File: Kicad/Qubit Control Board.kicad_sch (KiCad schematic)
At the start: 152 parts, among them J1 USB_C_Receptacle_PowerOnly_6P, J2 CLK_Pins, J3 Idata, J4 Qdata, J5 SPIdata, J6 SMA, U1 LT3045xMSE, U2 TRF372017IRGZR, U3 LT3045xMSE, U4 LT3045xMSE, U5 SN65LVDS1DBV, U6 AD9743BCPZ, Y2 CVHD-950-100.000

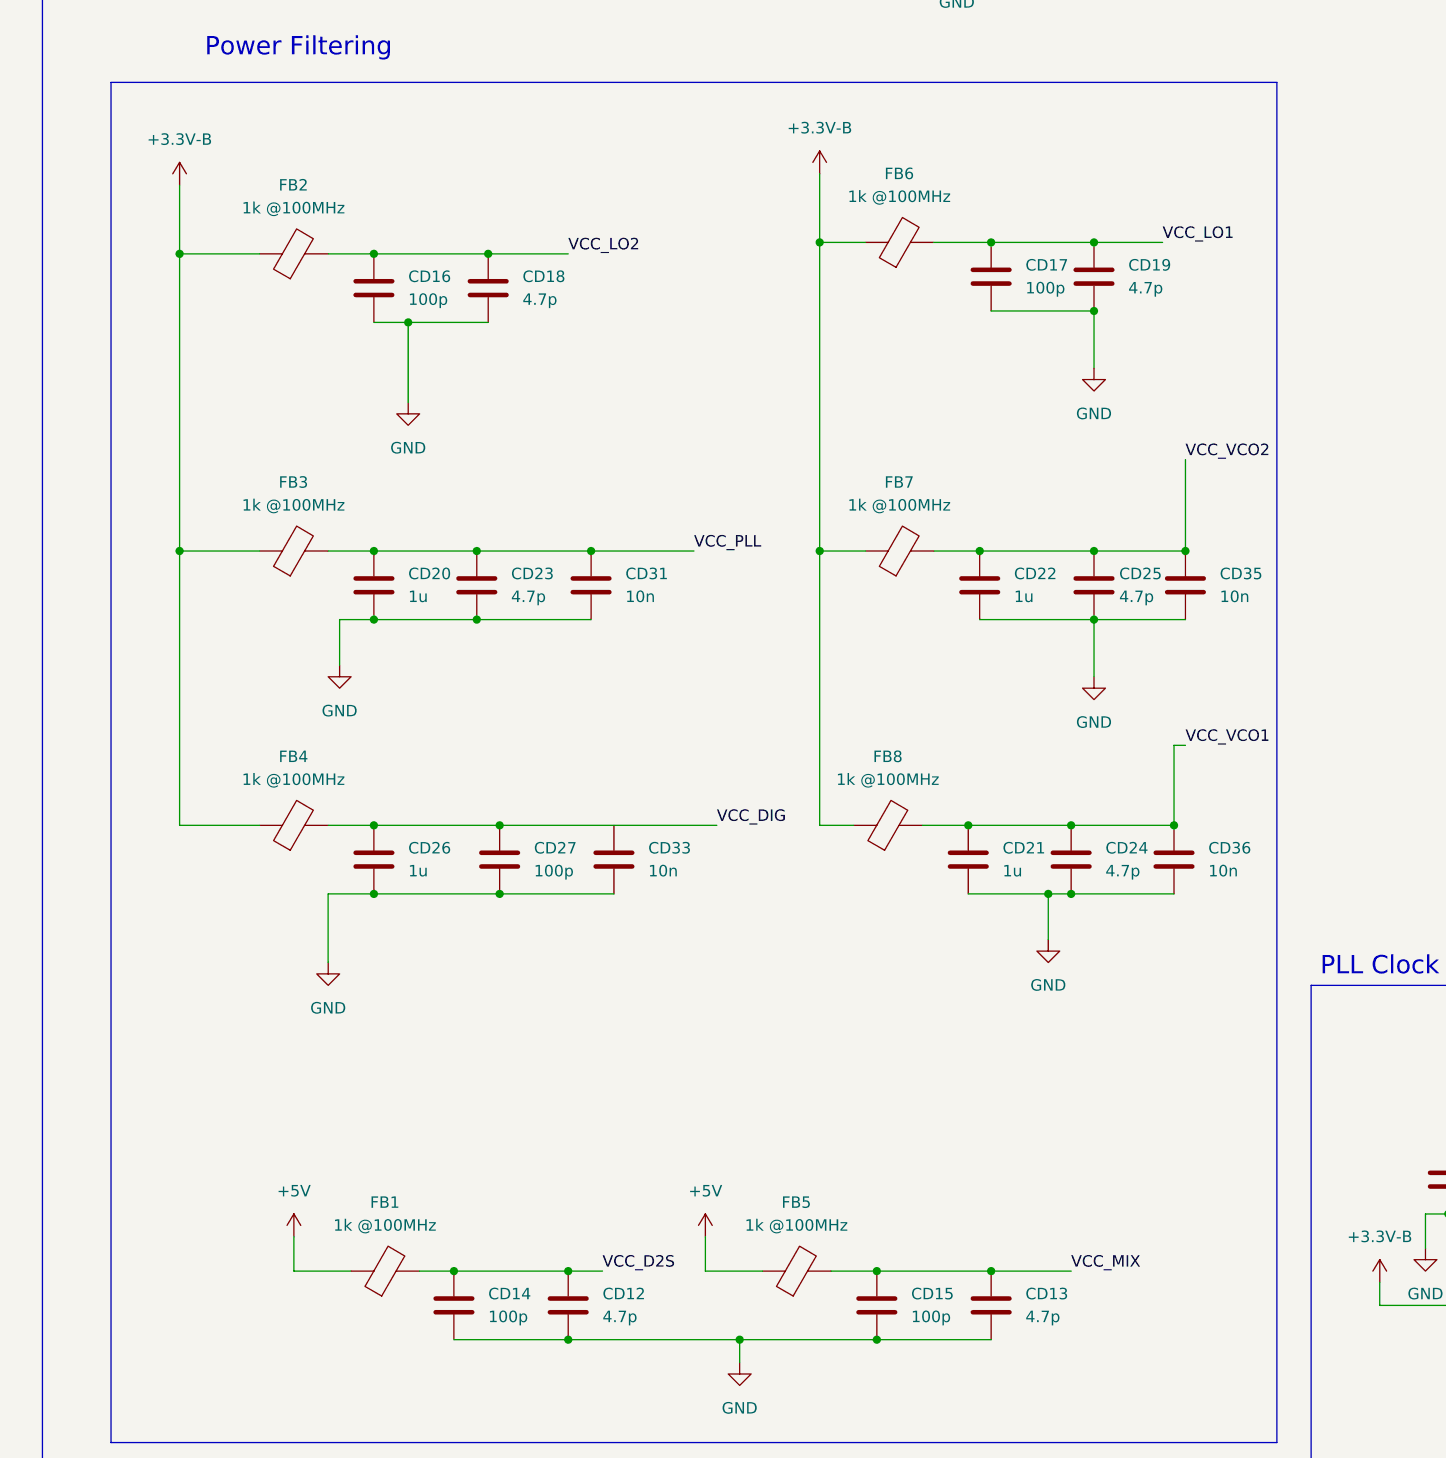
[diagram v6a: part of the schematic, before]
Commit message: added series R to FB to add damping to oss
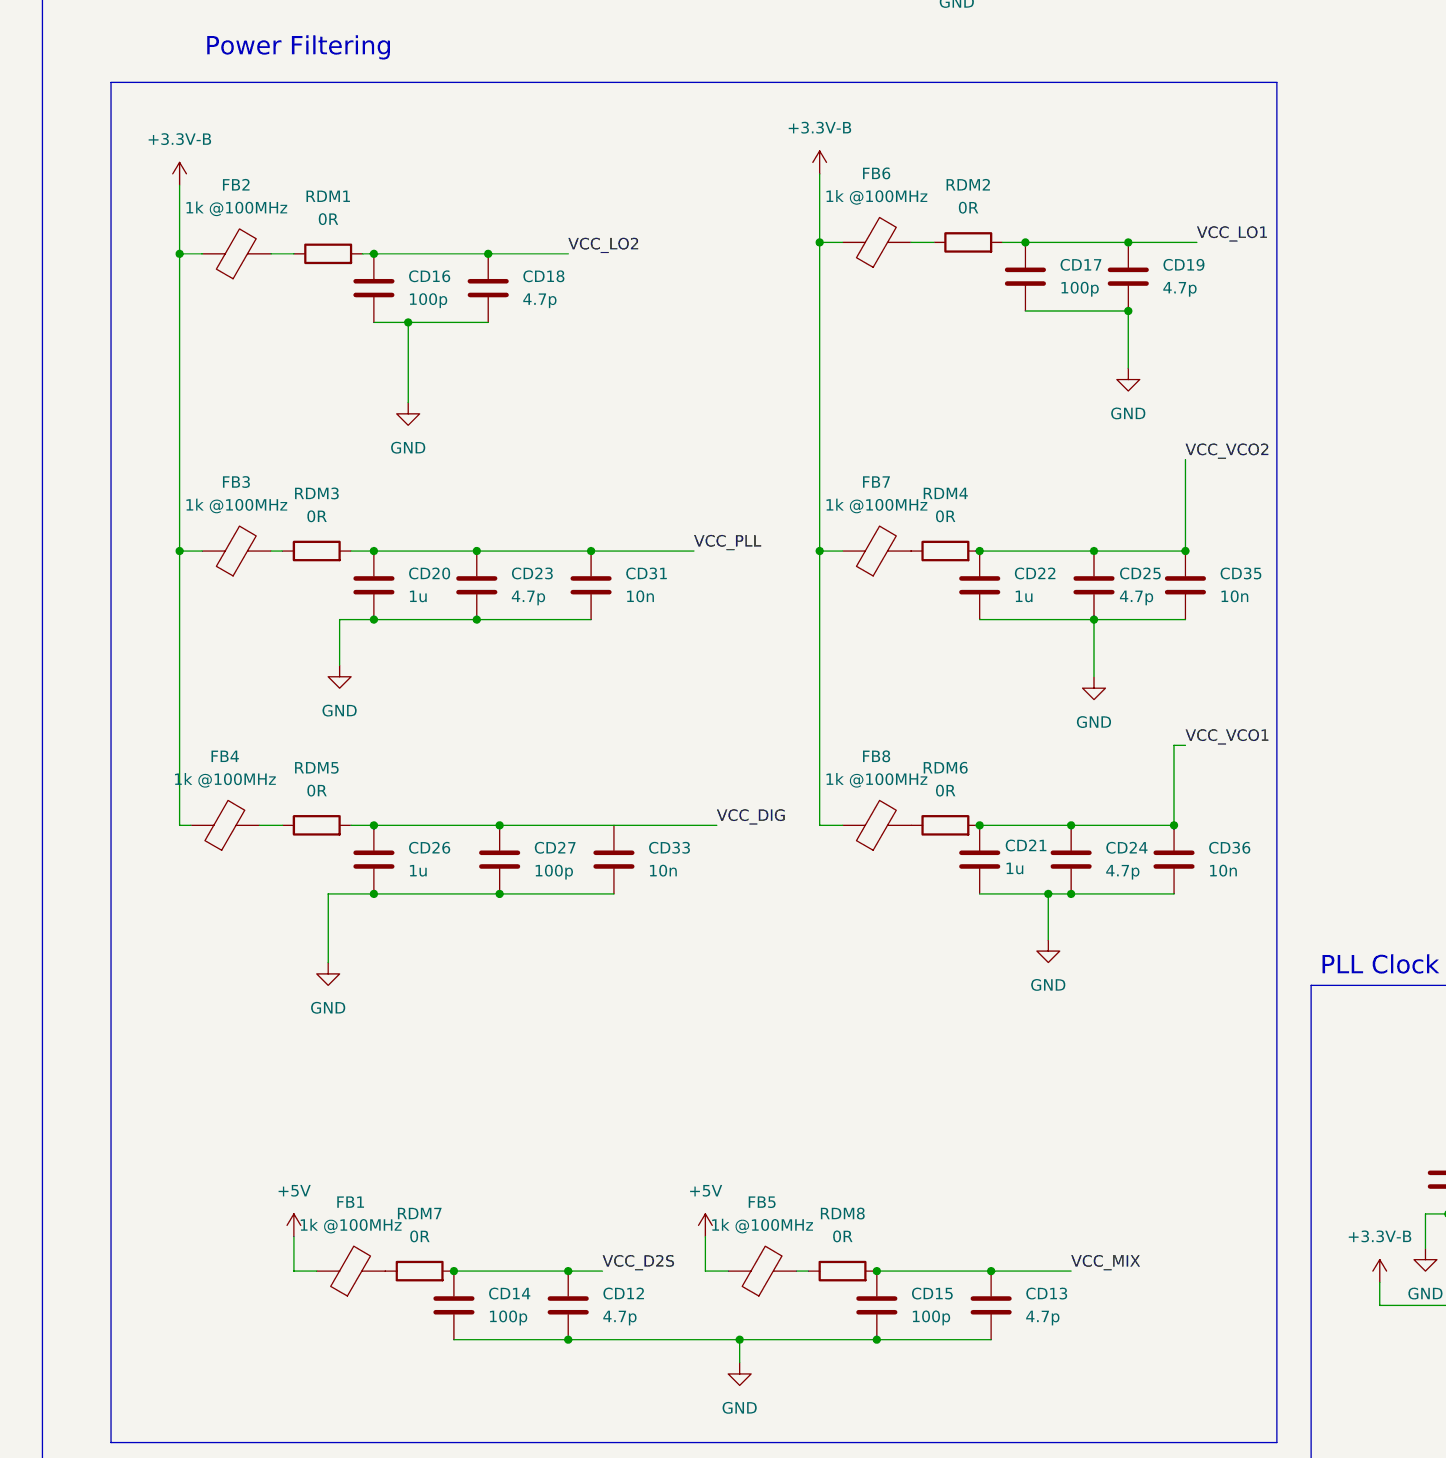
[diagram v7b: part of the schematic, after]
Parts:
- added RDM1, RDM2, RDM3, RDM4, RDM5, RDM6, RDM7, RDM8: 0R, Resistor_SMD:R_0603_1608Metric, symbol Device:R
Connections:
- net VCC_D2S: now also RDM7.2; no longer FB1.2
- net VCC_DIG: now also RDM5.2; no longer FB4.2
- net VCC_LO1: now also RDM2.2; no longer FB6.2
- net VCC_LO2: now also RDM1.2; no longer FB2.2
- net VCC_MIX: now also RDM8.2; no longer FB5.2
- net VCC_PLL: now also RDM3.2; no longer FB3.2
- net VCC_VCO1: now also RDM6.2; no longer FB8.2
- net VCC_VCO2: now also RDM4.2; no longer FB7.2
- new net: FB6.2, RDM2.1
- new net: FB7.2, RDM4.1
- new net: FB5.2, RDM8.1
- new net: FB2.2, RDM1.1
- new net: FB1.2, RDM7.1
- new net: FB4.2, RDM5.1
- new net: FB3.2, RDM3.1
- new net: FB8.2, RDM6.1
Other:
- moved on the sheet: CD17, CD19, CD21, FB1, FB2, FB3, FB4, FB5, FB6, FB7, FB8

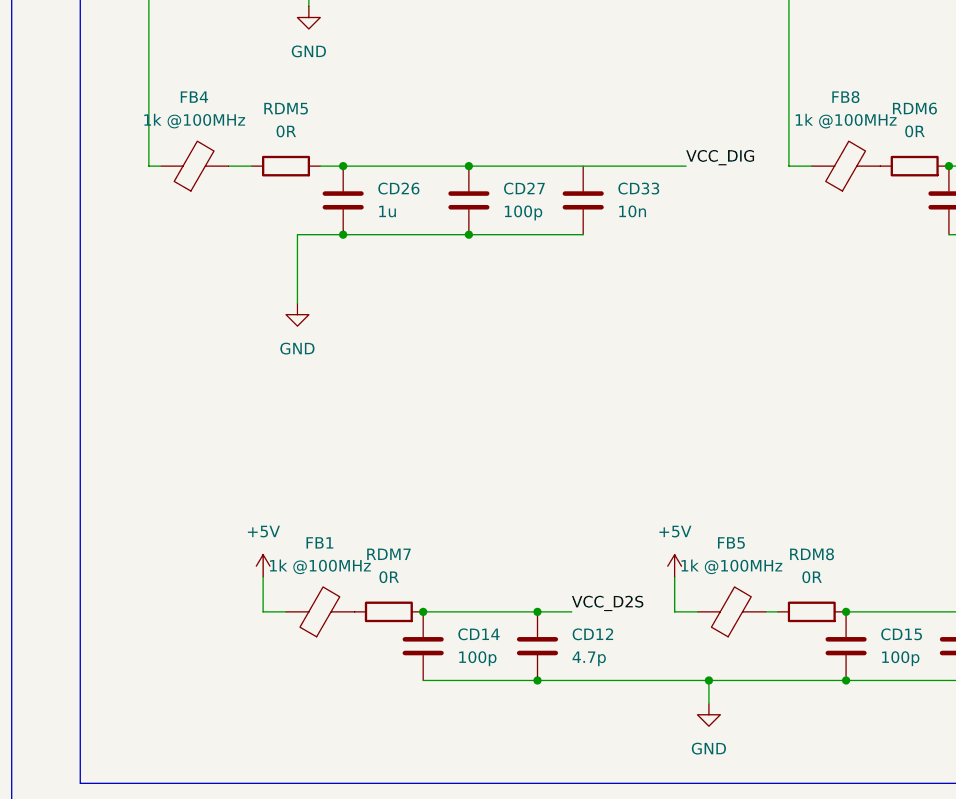
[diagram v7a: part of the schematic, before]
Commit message: REREF routing with on board clock
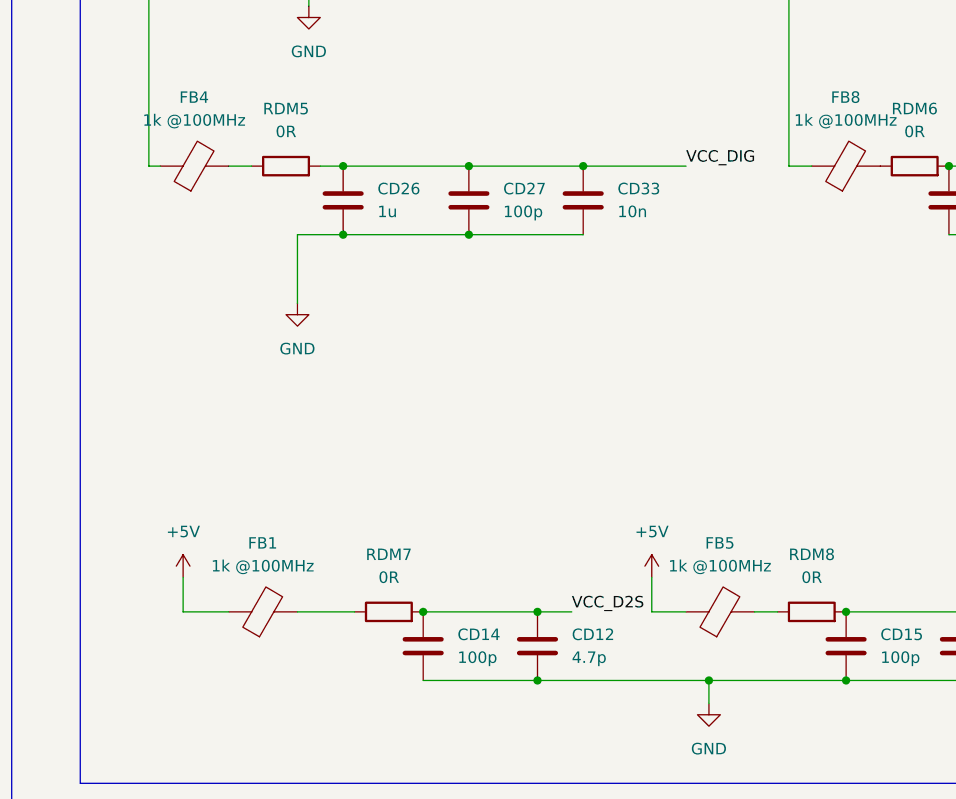
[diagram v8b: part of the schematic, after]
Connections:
- net VCC_DIG: now also CD33.2
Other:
- moved on the sheet: FB1, FB5
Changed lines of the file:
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@@
 	)
 	(junction
-		(at 379.73 294.64)
-		(diameter 0)
-		(color 0 0 0 0)
-	)
-	(junction
 		(at 509.27 185.42)
 		(diameter 0)
@@
 	)
 	(junction
+		(at 379.73 294.64)
+		(diameter 0)
+		(color 0 0 0 0)
+	)
+	(junction
 		(at 128.27 54.61)
 		(diameter 0)
@@
 	)
 	(junction
+		(at 392.43 287.02)
+		(diameter 0)
+		(color 0 0 0 0)
+	)
+	(junction
 		(at 55.88 200.66)
 		(diameter 0)
@@
 	(wire
 		(pts
-			(xy 356.87 332.74) (xy 356.87 336.55)
+			(xy 347.98 332.74) (xy 347.98 336.55)
 		)
 		(stroke
@@
 	(wire
 		(pts
-			(xy 402.59 336.55) (xy 405.13 336.55)
+			(xy 400.05 336.55) (xy 403.86 336.55)
 		)
 		(stroke
@@
 	(wire
 		(pts
+			(xy 360.68 336.55) (xy 367.03 336.55)
+		)
+		(stroke
+			(width 0)
+			(type default)
+		)
+	)
+	(wire
+		(pts
 			(xy 344.17 223.52) (xy 346.71 223.52)
 		)
@@
 	(wire
 		(pts
-			(xy 412.75 336.55) (xy 414.02 336.55)
+			(xy 411.48 336.55) (xy 414.02 336.55)
 		)
 		(stroke
@@
 	(wire
 		(pts
-			(xy 356.87 336.55) (xy 359.41 336.55)
+			(xy 347.98 336.55) (xy 353.06 336.55)
 		)
 		(stroke
@@
 	(wire
 		(pts
+			(xy 392.43 287.02) (xy 403.86 287.02)
+		)
+		(stroke
+			(width 0)
+			(type default)
+		)
+	)
+	(wire
+		(pts
 			(xy 80.01 355.6) (xy 86.36 355.6)
 		)
@@
 	(wire
 		(pts
-			(xy 379.73 287.02) (xy 403.86 287.02)
+			(xy 379.73 287.02) (xy 392.43 287.02)
 		)
 		(stroke
@@
 	(wire
 		(pts
-			(xy 402.59 332.74) (xy 402.59 336.55)
+			(xy 400.05 332.74) (xy 400.05 336.55)
 		)
 		(stroke
@@
 	(symbol
 		(lib_id "Device:FerriteBead")
-		(at 363.22 336.55 90)
+		(at 356.87 336.55 90)
 		(unit 1)
 		(body_style 1)
@@
 		(fields_autoplaced yes)
 		(property "Reference" "FB1"
-			(at 363.1692 328.93 90)
+			(at 356.8192 328.93 90)
 			(show_name no)
 			(do_not_autoplace no)
@@
 		)
 		(property "Value" "1k @100MHz"
-			(at 363.1692 331.47 90)
+			(at 356.8192 331.47 90)
 			(show_name no)
 			(do_not_autoplace no)
@@
 		)
 		(property "Footprint" "Inductor_SMD:L_0603_1608Metric_Pad1.05x0.95mm_HandSolder"
-			(at 363.22 338.328 90)
+			(at 356.87 338.328 90)
 			(hide yes)
 			(show_name no)
@@
 		)
 		(property "Datasheet" ""
-			(at 363.22 336.55 0)
+			(at 356.87 336.55 0)
 			(hide yes)
 			(show_name no)
@@
 		)
 		(property "Description" "Ferrite bead"
-			(at 363.22 336.55 0)
+			(at 356.87 336.55 0)
 			(hide yes)
 			(show_name no)
@@
 	(symbol
 		(lib_id "Device:FerriteBead")
-		(at 408.94 336.55 90)
+		(at 407.67 336.55 90)
 		(unit 1)
 		(body_style 1)
@@
 		(fields_autoplaced yes)
 		(property "Reference" "FB5"
-			(at 408.8892 328.93 90)
+			(at 407.6192 328.93 90)
 			(show_name no)
 			(do_not_autoplace no)
@@
 		)
 		(property "Value" "1k @100MHz"
-			(at 408.8892 331.47 90)
+			(at 407.6192 331.47 90)
 			(show_name no)
 			(do_not_autoplace no)
@@
 		)
 		(property "Footprint" "Inductor_SMD:L_0603_1608Metric_Pad1.05x0.95mm_HandSolder"
-			(at 408.94 338.328 90)
+			(at 407.67 338.328 90)
 			(hide yes)
 			(show_name no)
@@
 		)
 		(property "Datasheet" ""
-			(at 408.94 336.55 0)
+			(at 407.67 336.55 0)
 			(hide yes)
 			(show_name no)
@@
 		)
 		(property "Description" "Ferrite bead"
-			(at 408.94 336.55 0)
+			(at 407.67 336.55 0)
 			(hide yes)
 			(show_name no)
@@
 	(symbol
 		(lib_id "power:+5V")
-		(at 402.59 332.74 0)
+		(at 400.05 332.74 0)
 		(unit 1)
 		(body_style 1)
@@
 		(fields_autoplaced yes)
 		(property "Reference" "#PWR021"
-			(at 402.59 336.55 0)
+			(at 400.05 336.55 0)
 			(hide yes)
 			(show_name no)
@@
 		)
 		(property "Value" "+5V"
-			(at 402.59 327.66 0)
+			(at 400.05 327.66 0)
 			(show_name no)
 			(do_not_autoplace no)
@@
 		)
 		(property "Footprint" ""
-			(at 402.59 332.74 0)
+			(at 400.05 332.74 0)
 			(hide yes)
 			(show_name no)
@@
 		)
 		(property "Datasheet" ""
-			(at 402.59 332.74 0)
+			(at 400.05 332.74 0)
 			(hide yes)
 			(show_name no)
@@
 		)
 		(property "Description" "Power symbol creates a global label with name \"+5V\""
-			(at 402.59 332.74 0)
+			(at 400.05 332.74 0)
 			(hide yes)
 			(show_name no)
@@
 	(symbol
 		(lib_id "power:+5V")
-		(at 356.87 332.74 0)
+		(at 347.98 332.74 0)
 		(unit 1)
 		(body_style 1)
@@
 		(fields_autoplaced yes)
 		(property "Reference" "#PWR020"
-			(at 356.87 336.55 0)
+			(at 347.98 336.55 0)
 			(hide yes)
 			(show_name no)
@@
 		)
 		(property "Value" "+5V"
-			(at 356.87 327.66 0)
+			(at 347.98 327.66 0)
 			(show_name no)
 			(do_not_autoplace no)
@@
 		)
 		(property "Footprint" ""
-			(at 356.87 332.74 0)
+			(at 347.98 332.74 0)
 			(hide yes)
 			(show_name no)
@@
 		)
 		(property "Datasheet" ""
-			(at 356.87 332.74 0)
+			(at 347.98 332.74 0)
 			(hide yes)
 			(show_name no)
@@
 		)
 		(property "Description" "Power symbol creates a global label with name \"+5V\""
-			(at 356.87 332.74 0)
+			(at 347.98 332.74 0)
 			(hide yes)
 			(show_name no)
